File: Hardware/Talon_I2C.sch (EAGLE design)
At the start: 93 parts, among them J1 CONN_TALON_REMOTE, J2 CONN_I2C_LOGGER, J3 CONN_I2C_LOGGER, J4 CONN_I2C_LOGGER, J5 CONN_I2C_LOGGER, Q1 2N7002, Q2 2N7002, Q3 2N7002, Q4 2N7002, Q5 AO3419, Q6 AO3419, Q7 AO3419, Q8 AO3419, U1 SN74HC04, U10 74HC4852, U11 SN74LVC1G3157SC70, U12 MCP3421A3, U13 FXMAR2102UMLP, U14 PCA9617WSON, U15 PCA9617WSON, U16 PCA9617WSON, U17 PCA9617WSON, U18 SN74AUP1G08DCK, U19 SN74AUP1G08DCK, U2 CD4044, U20 SN74AUP1G08DCK, U21 SN74AUP1G08DCK, U3 SIP32431TDFN, U4 INA4180A2, U5 MAX9034TSSOP, U6 SN74AC08, U7 AT24MAC602SOT23, U8 MCP23018QFN, U9 PCA9536DFN

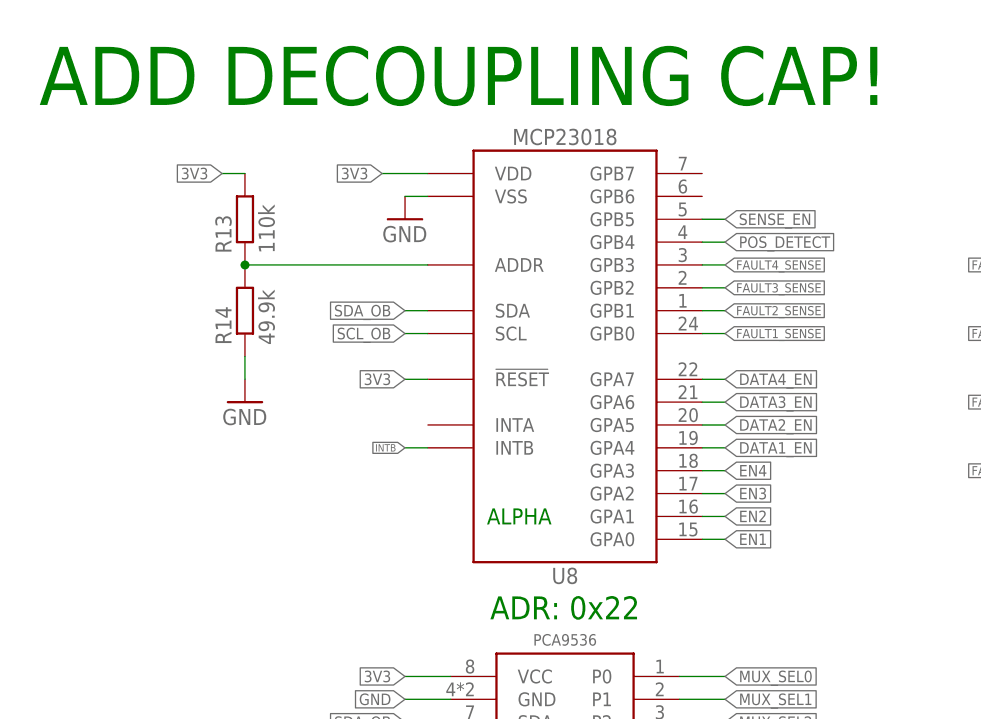
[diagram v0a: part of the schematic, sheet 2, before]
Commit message: v2.1 updates
Updates made to schematic and layout, boards sent to fab
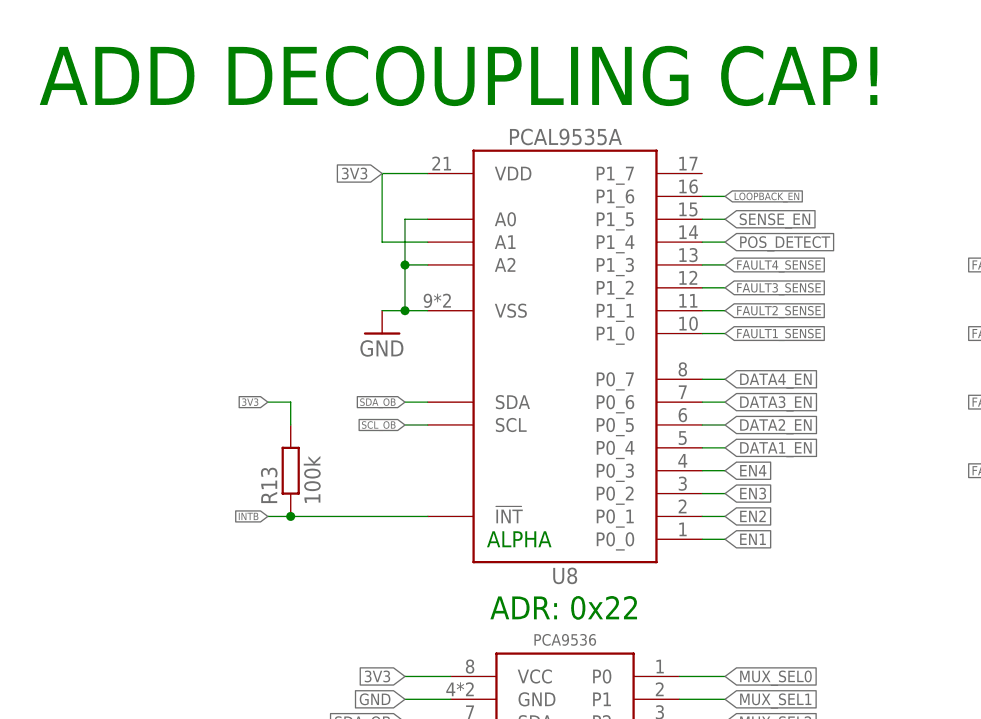
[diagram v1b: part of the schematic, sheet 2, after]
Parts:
- removed R14: 49.9k, bschulz_passives:R-EU_49.9KR0603
- added U22: SN74AUP1G32DCK, bschulz:SN74AUP1G32DCK
- R13: value 110k -> 100k; device bschulz_passives:R-EU_110KR0603 -> bschulz_passives:R-EU_100KR0402
- U8: value MCP23018QFN -> PCAL9535AQFN; device bschulz:MCP23018QFN -> bschulz:PCAL9535AQFN
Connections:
- removed net N$14: R13.1, R14.2, U8.ADDR
- new net LOOPBACK_EN: U22.A, U8.P1_6
- new net N$7: U13.EN, U22.Y
- net 3V3: now also U22.VCC, U8.A1; no longer U8.!RESET
- net DATA1_EN: now also U8.P0_4; no longer U8.GPA4
- net DATA2_EN: now also U8.P0_5; no longer U8.GPA5
- net DATA3_EN: now also U8.P0_6; no longer U8.GPA6
- net DATA4_EN: now also U8.P0_7; no longer U8.GPA7
- net EN1: now also U8.P0_0; no longer U8.GPA0
- net EN2: now also U8.P0_1; no longer U8.GPA1
- net EN3: now also U8.P0_2; no longer U8.GPA2
- net EN4: now also U8.P0_3; no longer U8.GPA3
- net FAULT1_SENSE: now also U8.P1_0; no longer U8.GPB0
- net FAULT2_SENSE: now also U8.P1_1; no longer U8.GPB1
- net FAULT3_SENSE: now also U8.P1_2; no longer U8.GPB2
- net FAULT4_SENSE: now also U8.P1_3; no longer U8.GPB3
- net GND: now also U22.GND, U8.A0, U8.A2; no longer R14.1
- net I2C_OB_EN: now also U22.B; no longer U13.EN
- net INTB: now also R13.1, U8.!INT; no longer U8.INTB
- net POS_DETECT: now also U8.P1_4; no longer U8.GPB4
- net SENSE_EN: now also U8.P1_5; no longer U8.GPB5
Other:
- moved on the sheet: C1, R13
